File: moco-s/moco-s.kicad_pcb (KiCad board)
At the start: 4 copper layers, 50 x 50 mm, 167 parts, among them J1 Conn_01x07, J2 Conn_01x02, J3 Conn_01x05, J5 Debug, J6 Conn_01x06, J7 Conn_01x03, J8 Conn_02x02_Top_Bottom, J9 Conn_02x02_Top_Bottom, Q1 AO3413, Q2 AO3413, Q3 CSD18540Q5B, Q4 CSD18540Q5B, Q5 CSD18540Q5B, Q6 CSD18540Q5B, Q7 CSD18540Q5B, Q8 CSD18540Q5B, SW1 SW_Push, SW2 SW_Push, U1 AMS1117-3.3, U2 DRV8301, U3 STM32G431CBT6, U4 MCP2515-xST, U5 TJA1051T-3, U6 AS5147, Y1 32.768kHz, Y2 8MHz, Y3 8MHz

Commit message: Update net classes
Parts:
- moved J7 1.50 mm to (147.5, 79.0)
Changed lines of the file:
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@@
   )
   (footprint "moco:AMASS MR30PB-F" (layer "F.Cu")
-    (at 147.5 77.5 -90)
+    (at 147.5 79 -90)
     (property "Note" "J7 connect to motor")
     (property "Sheetfile" "File: motor_driver.kicad_sch")

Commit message: Update layout
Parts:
- removed J6: Conn_01x06, Connector_JST:JST_GH_SM06B-GHS-TB_1x06-1MP_P1.25mm_Horizontal
- removed JP4, JP5, SB15, SB20: SolderJumper_3_Bridged12, Jumper:SolderJumper-3_P1.3mm_Bridged12_RoundedPad1.0x1.5mm_NumberLabels
- removed R19, R20, R21: 3.3k, Resistor_SMD:R_0402_1005Metric
- removed SB14, SB21, SB22: SolderJumper_2_Bridged, Jumper:SolderJumper-2_P1.3mm_Bridged_RoundedPad1.0x1.5mm
- removed TP1, TP2: TestPoint, TestPoint:TestPoint_Pad_D2.0mm
- added R14: 3.3k, Resistor_SMD:R_0402_1005Metric, F.Cu at (95.6, 68.5)
- added R17: 3.3k, Resistor_SMD:R_0402_1005Metric, F.Cu at (91.2, 72.0)
- added R18: 3.3k, Resistor_SMD:R_0402_1005Metric, F.Cu at (94.2, 72.0)
- J3: value Conn_01x05 -> Conn_01x09; footprint Connector_JST:JST_GH_SM05B-GHS-TB_1x05-1MP_P1.25mm_Horizontal -> Connector_JST:JST_GH_SM09B-GHS-TB_1x09-1MP_P1.25mm_Horizontal
- NT2: moved to B.Cu
- SB4: value SolderJumper_3_Bridged12 -> SolderJumper_2_Bridged; footprint Jumper:SolderJumper-3_P1.3mm_Bridged12_RoundedPad1.0x1.5mm_NumberLabels -> Jumper:SolderJumper-2_P1.3mm_Bridged_RoundedPad1.0x1.5mm; moved to F.Cu
- moved SB4 26.6 mm to (92.0, 69.3), turned to 0 degrees
- moved C1 21.1 mm to (160.0, 67.2)
- moved C3 21.1 mm to (160.0, 79.2)
- moved C32 21.1 mm to (160.0, 91.2)
- moved C33 21.1 mm to (160.0, 83.2)
- moved C35 21.1 mm to (160.0, 75.2)
- moved C4 21.1 mm to (160.0, 71.2)
- moved C5 21.1 mm to (160.0, 63.2)
- moved C7 21.1 mm to (160.0, 87.2)
- moved R24 12.2 mm to (142.0, 60.2), turned to 0 degrees
- moved C37 10.5 mm to (125.6, 92.0), turned to 180 degrees
- moved C38 10.4 mm to (125.6, 89.6), turned to 0 degrees
- moved R13 8.73 mm to (121.7, 98.5), turned to 180 degrees
- moved SB7 6.20 mm to (108.8, 94.6)
- moved Y1 6.09 mm to (122.6, 90.8), turned to 90 degrees
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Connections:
- J1 pad 1: Net-(J1-Pad1) -> VCC
- J3 pad 1: Net-(J3-Pad1) -> VCC
- J3 pad 5: GND -> /SPI_CLK
- SB4 pad 1: VCC -> Net-(R14-Pad1)
- SB4 pad 2: Net-(J1-Pad1) -> VCC
- U3 pad 33: /CAN BUS/CNA_RX -> /CAN BUS/~{INT}
- U3 pad 46: /CAN BUS/CNA_TX -> /CAN BUS/SPI_~{CS}
- U4 pad 1: /CAN BUS/MCP_TX -> /CAN BUS/TX
- U4 pad 13: Net-(SB22-Pad1) -> /CAN BUS/~{INT}
- U4 pad 18: Net-(SB21-Pad2) -> /CAN BUS/SPI_~{CS}
- U4 pad 2: /CAN BUS/MCP_RX -> /CAN BUS/RX
- U5 pad 1: /CAN BUS/CAN_TX_TRN -> /CAN BUS/TX
- U5 pad 4: /CAN BUS/CAN_RX_TRN -> /CAN BUS/RX
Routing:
- net GND: track 0.00 -> 79.5 mm, vias 0 -> 35
- net VCC: track 0.00 -> 76.2 mm, vias 0 -> 12
- net /SPI_MOSI: track 0.00 -> 68.5 mm, vias 0 -> 4
- net /ENC_B: track 0.00 -> 59.9 mm, vias 0 -> 2
- net /EN_GATE: track 0.00 -> 58.0 mm, vias 0 -> 3
- net /~{OCTW}: track 0.00 -> 57.3 mm, vias 0 -> 4
- net /ENC_I: track 0.00 -> 55.6 mm, vias 0 -> 2
- net /SPI_CLK: track 0.00 -> 53.8 mm, vias 0 -> 4
- net /ENC_A: track 0.00 -> 51.6 mm, vias 0 -> 2
- net /SPI_MISO: track 0.00 -> 51.1 mm, vias 0 -> 3
- net Vdrive: track 0.00 -> 48.8 mm, vias 0 -> 17
- net /~{FAULT}: track 0.00 -> 47.1 mm, vias 0 -> 3
- net /MCU/TEMP_SENSE: track 0.00 -> 40.7 mm, vias 0 -> 2
- net +5V: track 0.00 -> 39.7 mm, vias 0 -> 2
- net /CAN BUS/SPI_~{CS}: track 0.00 -> 36.5 mm, vias 0 -> 2
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- added copper zone on B.Cu, net /Motor Driver/MOTOR_A
- added copper zone on F.Cu, net /Motor Driver/MOTOR_A
- added copper zone on B.Cu, net /Motor Driver/MOTOR_B
- added copper zone on F.Cu, net /Motor Driver/MOTOR_B
- added copper zone on B.Cu, net /Motor Driver/MOTOR_C
- added copper zone on F.Cu, net /Motor Driver/MOTOR_C
- added copper zone on B.Cu, net /Motor Driver/SL_B
- added copper zone on F.Cu, net /Motor Driver/SL_B
- added copper zone on B.Cu, net /Motor Driver/SL_C
- added copper zone on F.Cu, net /Motor Driver/SL_C
- added copper zone on B.Cu, net GND
- added copper zone on F.Cu, net GND
- added copper zone on In1.Cu, net GND
- added copper zone on B.Cu, net Vdrive
- added copper zone on F.Cu, net Vdrive
- added copper zone on In1.Cu, net Vdrive

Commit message: Comp MoCo-S
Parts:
- removed C37, C38: 12pF, Capacitor_SMD:C_0603_1608Metric
- removed C4: 22uF/50V, Capacitor_SMD:C_1210_3225Metric_Pad1.33x2.70mm_HandSolder
- removed C52: 100nF, Capacitor_SMD:C_0402_1005Metric
- removed C53: 100pF, Capacitor_SMD:C_0402_1005Metric
- removed LD2, LD3, LD4, LD5: LED, LED_SMD:LED_0603_1608Metric
- removed Q1, Q2: AO3413, Package_TO_SOT_SMD:SOT-23
- removed R10, R5: 330R, Resistor_SMD:R_0402_1005Metric
- removed R12, R51: 10k, Resistor_SMD:R_0603_1608Metric
- removed R23: 1k, Resistor_SMD:R_0402_1005Metric
- removed R4, R47, R48, R9: 10k, Resistor_SMD:R_0402_1005Metric
- removed R49: 120R, Resistor_SMD:R_0402_1005Metric
- removed R7: 150R, Resistor_SMD:R_0402_1005Metric
- removed SB1, SB19, SB2, SB3, SB6: SolderJumper_2_Bridged, Jumper:SolderJumper-2_P1.3mm_Bridged_RoundedPad1.0x1.5mm
- removed U5: TJA1051T-3, Package_SO:SOIC-8_3.9x4.9mm_P1.27mm
- removed Y1: 32.768kHz, Crystal:Crystal_SMD_3215-2Pin_3.2x1.5mm
- added R19: 10k, Resistor_SMD:R_0402_1005Metric, F.Cu at (105.9, 95.3)
- added R20: 120R, Resistor_SMD:R_0402_1005Metric, F.Cu at (105.5, 85.2)
- added SB5: SolderJumper_2_Open, Jumper:SolderJumper-2_P1.3mm_Open_TrianglePad1.0x1.5mm, B.Cu at (106.2, 83.5)
- C47, C48: value 12pF -> 100nF
- C50: value 100nF -> 22pF
- C51: value 10uF -> 22pF; footprint Capacitor_Tantalum_SMD:CP_EIA-3216-18_Kemet-A -> Capacitor_SMD:C_0402_1005Metric
- C8: value 10uF -> 4.7uF; footprint Capacitor_Tantalum_SMD:CP_EIA-3216-18_Kemet-A -> Capacitor_SMD:C_0402_1005Metric
- H1, H2: footprint MountingHole:MountingHole_3.2mm_M3_Pad_Via -> MountingHole:MountingHole_2.2mm_M2_Pad_Via
- H3, H4: footprint MountingHole:MountingHole_3.2mm_M3_ISO14580 -> MountingHole:MountingHole_2.2mm_M2_ISO14580
- J1: value Conn_01x07 -> Conn_01x06; footprint Connector_JST:JST_GH_SM07B-GHS-TB_1x07-1MP_P1.25mm_Horizontal -> Connector_JST:JST_GH_SM06B-GHS-TB_1x06-1MP_P1.25mm_Horizontal
- J3, NT2: moved to F.Cu
- J9, SB4: moved to B.Cu
- LD1: value LED -> LED_BAGR; footprint LED_SMD:LED_0603_1608Metric -> moco:RGB LED 1.6x1.6mm
- R1: value 1k -> 560R
- R2: value 1k -> 330R
- R3: value 150R -> 330R
- U1: value AMS1117-3.3 -> XC6220B331MR; footprint Package_TO_SOT_SMD:SOT-223-3_TabPin2 -> Package_TO_SOT_SMD:SOT-23-5
- U4: value MCP2515-xST -> MCP25625; footprint Package_SO:TSSOP-20_4.4x6.5mm_P0.65mm -> Package_DFN_QFN:QFN-28-1EP_6x6mm_P0.65mm_EP4.25x4.25mm
- Y3: value 8MHz -> 16MHz; footprint Crystal:Crystal_SMD_Qantek_QC5CB-2Pin_5x3.2mm -> Crystal:Crystal_SMD_3225-4Pin_3.2x2.5mm
- moved R2 45.5 mm to (109.0, 98.2), turned to 0 degrees
- moved R3 40.7 mm to (109.0, 99.2), turned to 0 degrees
- moved R11 36.7 mm to (107.7, 63.1), turned to 180 degrees
- moved R6 35.0 mm to (107.7, 64.4), turned to 180 degrees
- moved C5 34.7 mm to (133.4, 85.6)
- moved C33 32.3 mm to (134.2, 63.8)
- moved SB7 30.9 mm to (109.5, 63.8), turned to 180 degrees
- moved C1 30.3 mm to (132.2, 79.3)
- moved C3 28.0 mm to (132.2, 75.9)
- moved C35 27.0 mm to (134.2, 67.2)
- moved C7 25.2 mm to (134.9, 89.9), turned to -90 degrees
- moved J1 23.4 mm to (103.2, 63.1)
- moved C32 21.8 mm to (138.2, 89.9), turned to -90 degrees
- moved R17 20.0 mm to (107.7, 60.6), turned to 180 degrees
- moved SB4 19.5 mm to (109.5, 60.6)
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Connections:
- net /GPIO_PB13 renamed /SPI_DRIVER_~{CS}
- net /GPIO_PB14 renamed /SPI_SENSOR_~{CS}
- C47 pad 1: GND -> VCC
- C47 pad 2: Net-(C47-Pad2) -> GND
- C48 pad 1: Net-(C48-Pad1) -> VCC
- C49 pad 1: VCC -> +5V
- C50 pad 1: VCC -> Net-(C50-Pad1)
- C51 pad 1: +5V -> GND
- C51 pad 2: GND -> Net-(C51-Pad2)
- J1 pad 4: /GPIO_PB0 -> /GPIO_PB2
- J1 pad 5: /GPIO_PB1 -> /GPIO_PB11
- J1 pad 6: /GPIO_PB2 -> GND
- J5 pad 3: GND -> /SWDIO
- J5 pad 4: /SWDIO -> GND
- LD1 pad 1: GND -> Net-(LD1-Pad1)
- LD1 pad 2: Net-(LD1-Pad2) -> +5V
- R1 pad 1: Net-(R1-Pad1) -> Net-(LD1-Pad4)
- R1 pad 2: Net-(LD1-Pad2) -> /USER_LED_1
- R2 pad 1: Net-(R2-Pad1) -> Net-(LD1-Pad3)
- R2 pad 2: Net-(LD2-Pad2) -> GND
- R3 pad 1: Net-(Q1-Pad1) -> Net-(LD1-Pad1)
- R3 pad 2: /~{OCTW} -> /USER_LED_2
- R31 pad 1: /~{OCTW} -> /Motor Driver/~{OCTW}
- U1 pad 1: GND -> +5V
- U1 pad 2: VCC -> GND
- U2 pad 5: /~{OCTW} -> /Motor Driver/~{OCTW}
- U3 pad 16: /GPIO_PB0 -> /USER_LED_1
- U3 pad 17: /GPIO_PB1 -> /USER_LED_2
- U3 pad 25: /~{OCTW} -> /GPIO_PB11
- U3 pad 3: Net-(C37-Pad2) -> unconnected-(U3-Pad3)
- U3 pad 4: Net-(C38-Pad1) -> unconnected-(U3-Pad4)
- U3 pad 46: /CAN BUS/SPI_~{CS} -> /SPI_CAN_~{CS}
- U4 pad 1: /CAN BUS/TX -> VCC
- U4 pad 15: unconnected-(U4-Pad15) -> /SPI_MOSI
- U4 pad 16: /SPI_MOSI -> /SPI_MISO
- U4 pad 17: /SPI_MISO -> /SPI_CAN_~{CS}
- U4 pad 18: /CAN BUS/SPI_~{CS} -> Net-(R19-Pad2)
- U4 pad 19: Net-(R47-Pad2) -> VCC
- U4 pad 2: /CAN BUS/RX -> unconnected-(U4-Pad2)
- U4 pad 20: VCC -> Net-(U4-Pad20)
- U4 pad 3: unconnected-(U4-Pad3) -> /CAN BUS/CAN_L
- U4 pad 4: unconnected-(U4-Pad4) -> /CAN BUS/CAN_H
- U4 pad 5: unconnected-(U4-Pad5) -> GND
- U4 pad 8: Net-(C47-Pad2) -> Net-(C50-Pad1)
- U4 pad 9: Net-(C48-Pad1) -> Net-(C51-Pad2)
- Y3 pad 1: Net-(C47-Pad2) -> Net-(C51-Pad2)
- Y3 pad 2: Net-(C48-Pad1) -> GND
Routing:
- net VCC: track 76.2 -> 261.9 mm, vias 12 -> 18
- net +5V: track 39.7 -> 110.7 mm, vias 2 -> 4
- net /~{OCTW}: track 57.3 -> 0.00 mm, vias 4 -> 0
- net /I2C_SDA: track 2.13 -> 50.9 mm, vias 0 -> 4
- net /GPIO_PB11: track 0.00 -> 43.0 mm, vias 0 -> 2
- net /I2C_SCL: track 1.92 -> 42.3 mm, vias 0 -> 3
- net /GPIO_PB2: track 7.61 -> 46.8 mm, vias 1 -> 2
- net /CAN BUS/SPI_~{CS}: track 36.5 -> 0.00 mm, vias 2 -> 0
- net /OnBoard_ENC_A: track 0.00 -> 32.3 mm, vias 0 -> 3
- net /SPI_CLK: track 53.8 -> 86.0 mm, vias 4 -> 5
- net /OnBoard_ENC_B: track 0.00 -> 31.6 mm, vias 0 -> 3
- net /SPI_MISO: track 51.1 -> 81.1 mm, vias 3 -> 5
- net /ENC_B: track 59.9 -> 32.0 mm
- net GND: track 79.5 -> 107.1 mm, vias 35 -> 107
- net /CAN BUS/CAN_L: track 21.0 -> 47.9 mm
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- removed copper zone on B.Cu, net /Motor Driver/SL_B
- removed copper zone on B.Cu, net /Motor Driver/SL_C
- removed copper zone on In1.Cu, net Vdrive

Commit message: Update ref
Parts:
- renumbered C2 to C1, C15 to C10, C16 to C11, C17 to C12, C18 to C13, C19 to C14, C20 to C15, C21 to C16, C22 to C17, C23 to C18, C24 to C19, C6 to C2, C25 to C20, C26 to C21, C27 to C22, C28 to C23, C29 to C24, C30 to C25, C36 to C26, C31 to C27, C5 to C28, C7 to C29, C8 to C3, C32 to C30, C33 to C31, C35 to C32, C34 to C33, C1 to C34, C3 to C35, C39 to C36, C40 to C37, C41 to C38, C42 to C39, C9 to C4, C43 to C40, C44 to C41, C45 to C42, C46 to C43, C47 to C44, C48 to C45, C49 to C46, C50 to C47, C51 to C48, C54 to C49, C10 to C5, C55 to C50, C11 to C6, C12 to C7, C13 to C8, C14 to C9, H3 to H1, H1 to H2, H4 to H3, H2 to H4, J5 to J2, J2 to J3, J3 to J4, J7 to J5, J8 to J6, J9 to J7, Q3 to Q1, Q4 to Q2, Q5 to Q3, Q6 to Q4, Q7 to Q5, Q8 to Q6, R6 to R1, R14 to R10, R17 to R11, R18 to R12, R24 to R13, R25 to R14, R26 to R15, R27 to R16, R28 to R17, R29 to R18, R30 to R19, R8 to R2, R31 to R20, R32 to R21, R33 to R22, R34 to R23, R35 to R24, R36 to R25, R37 to R26, R38 to R27, R39 to R28, R40 to R29, R11 to R3, R41 to R30, R42 to R31, R43 to R32, R44 to R33, R45 to R34, R46 to R35, R19 to R36, R20 to R37, R52 to R38, R15 to R4, R16 to R5, R13 to R6, R1 to R7, R2 to R8, R3 to R9, SB7 to SB1, JP1 to SB2, JP2 to SB3, JP3 to SB4, SB4 to SB5, SB5 to SB6, TP3 to TP1, TP5 to TP2, TP4 to TP3, U6 to U5, Y2 to Y1, Y3 to Y2

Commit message: Update layout
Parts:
- added kibuzzard-638C8B7C: G***, kibuzzard-638C8B7C, B.Cu at (139.7, 59.2)
- added kibuzzard-638C8BCF: G***, kibuzzard-638C8BCF, B.Cu at (132.6, 58.7)
- added kibuzzard-638C8E29: G***, kibuzzard-638C8E29, B.Cu at (109.9, 72.4)
- added kibuzzard-638C8E4D: G***, kibuzzard-638C8E4D, B.Cu at (111.5, 75.2)
- moved C2 0.25 mm to (117.9, 52.4)
- moved C3 0.25 mm to (117.9, 54.6)
- moved U1 0.25 mm to (115.6, 53.5)
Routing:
- net VCC: track 261.9 -> 259.0 mm
- net GND: track 107.1 -> 104.5 mm, vias 107 -> 118
- net Net-(C19-Pad2): track 22.7 -> 21.6 mm
- net Vdrive: track 48.7 -> 49.2 mm, vias 122 -> 133
- net /Motor Driver/MOTOR_B: track 25.1 -> 24.8 mm, vias 43 -> 49
- net /Motor Driver/MOTOR_C: vias 43 -> 50
- net /Motor Driver/MOTOR_A: vias 43 -> 50
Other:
- outline, holes or cut-outs redrawn

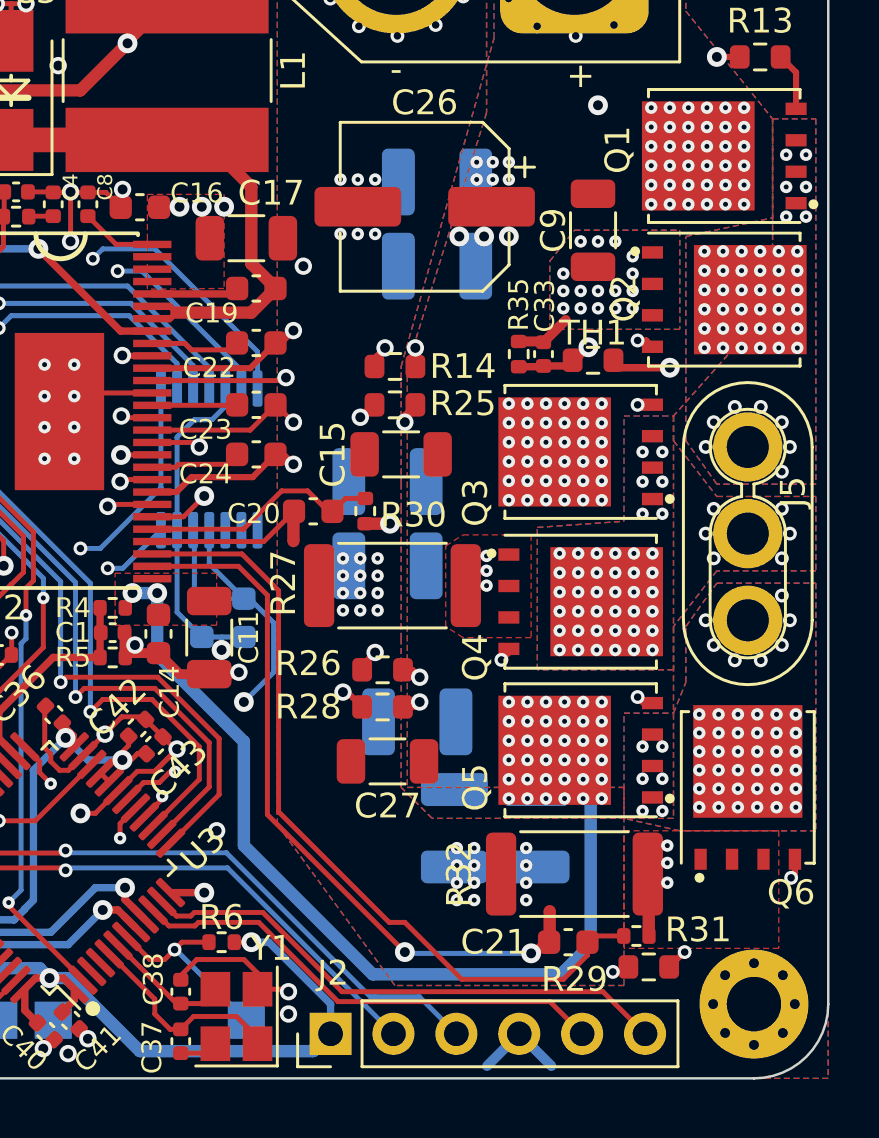
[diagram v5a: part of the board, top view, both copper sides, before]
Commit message: Use kelvin connection for shunt resistance
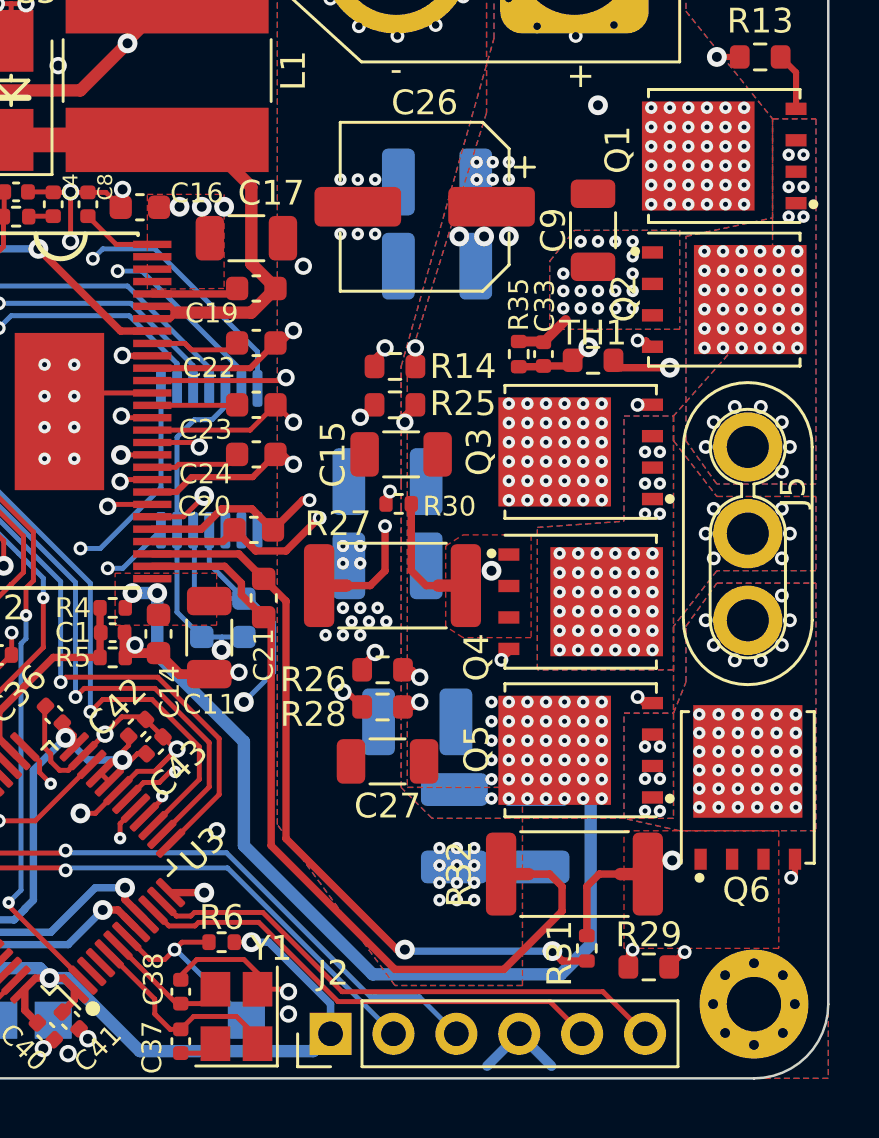
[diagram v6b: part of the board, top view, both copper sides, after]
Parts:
- C43: value 1uF/25V -> 1uF
- moved C21 18.6 mm to (127.2, 80.6), turned to -90 degrees
- moved NT1 3.87 mm to (134.8, 80.1)
- moved NT2 2.83 mm to (130.1, 80.1), turned to 180 degrees
- moved C20 2.51 mm to (126.8, 77.8)
- moved NT4 2.41 mm to (137.4, 91.8), turned to 180 degrees
- moved R31 2.06 mm to (140.2, 94.8), turned to 90 degrees
- moved NT3 1.87 mm to (142.1, 91.8), turned to 0 degrees
- moved R30 1.38 mm to (132.7, 76.8), turned to 0 degrees
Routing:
- net /Motor Driver/SP1: track 6.44 -> 14.2 mm, vias 0 -> 2
- net /Motor Driver/SP2: track 27.9 -> 32.3 mm, vias 2 -> 0
- net /Motor Driver/SN1: track 0.00 -> 4.04 mm
- net /Motor Driver/SN2: track 0.00 -> 3.55 mm
- net Net-(C21-Pad1): track 32.4 -> 30.0 mm, vias 0 -> 2
- net /Motor Driver/GL_C: track 37.5 -> 35.5 mm
- net Net-(C20-Pad1): track 9.80 -> 11.5 mm, vias 0 -> 2
- net /Motor Driver/SL_C: track 31.3 -> 29.7 mm, vias 4 -> 2
- net /GPIO_PB2: track 46.7 -> 47.5 mm
- net /Motor Driver/SL_B: track 19.9 -> 20.1 mm, vias 5 -> 2
- net Vdrive: vias 133 -> 139
- net GND: vias 118 -> 120
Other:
- board text added: "${TITLE} v${REVISION}"

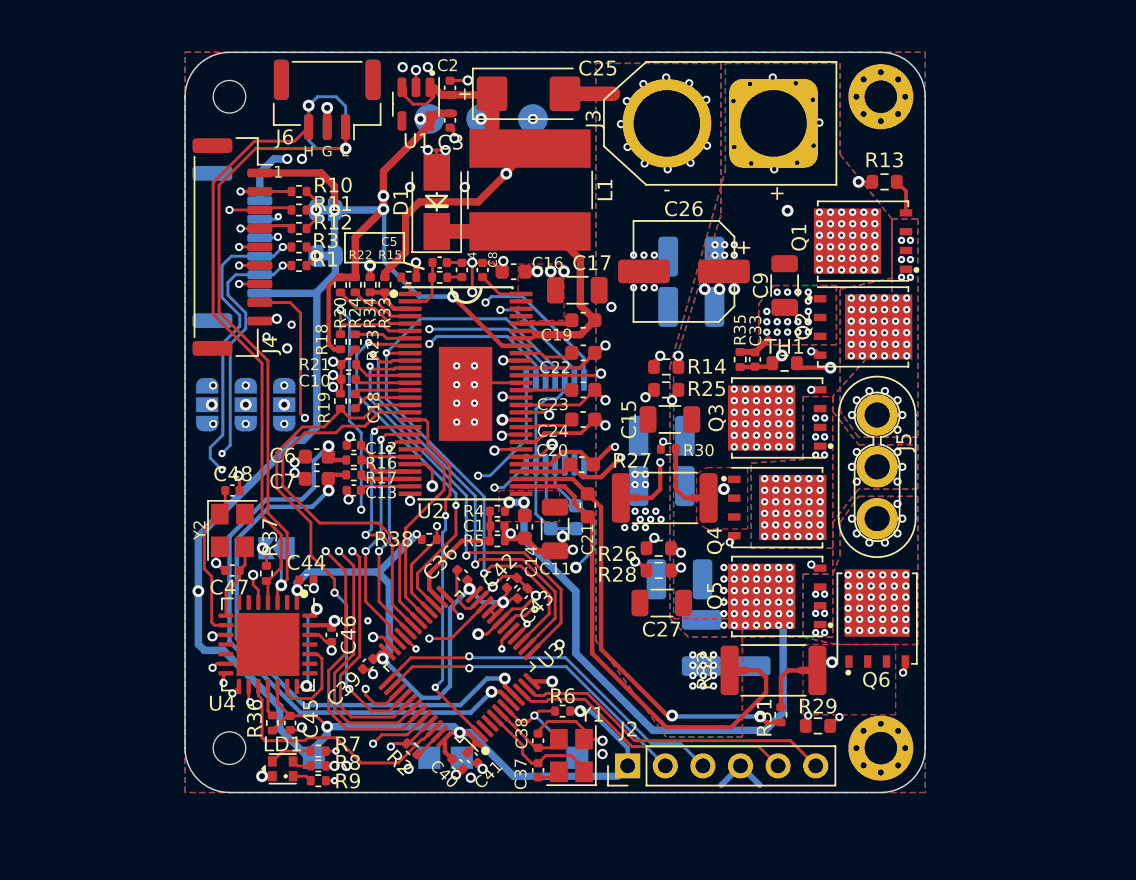
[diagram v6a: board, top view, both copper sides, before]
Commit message: Replace some extended parts to basic parts
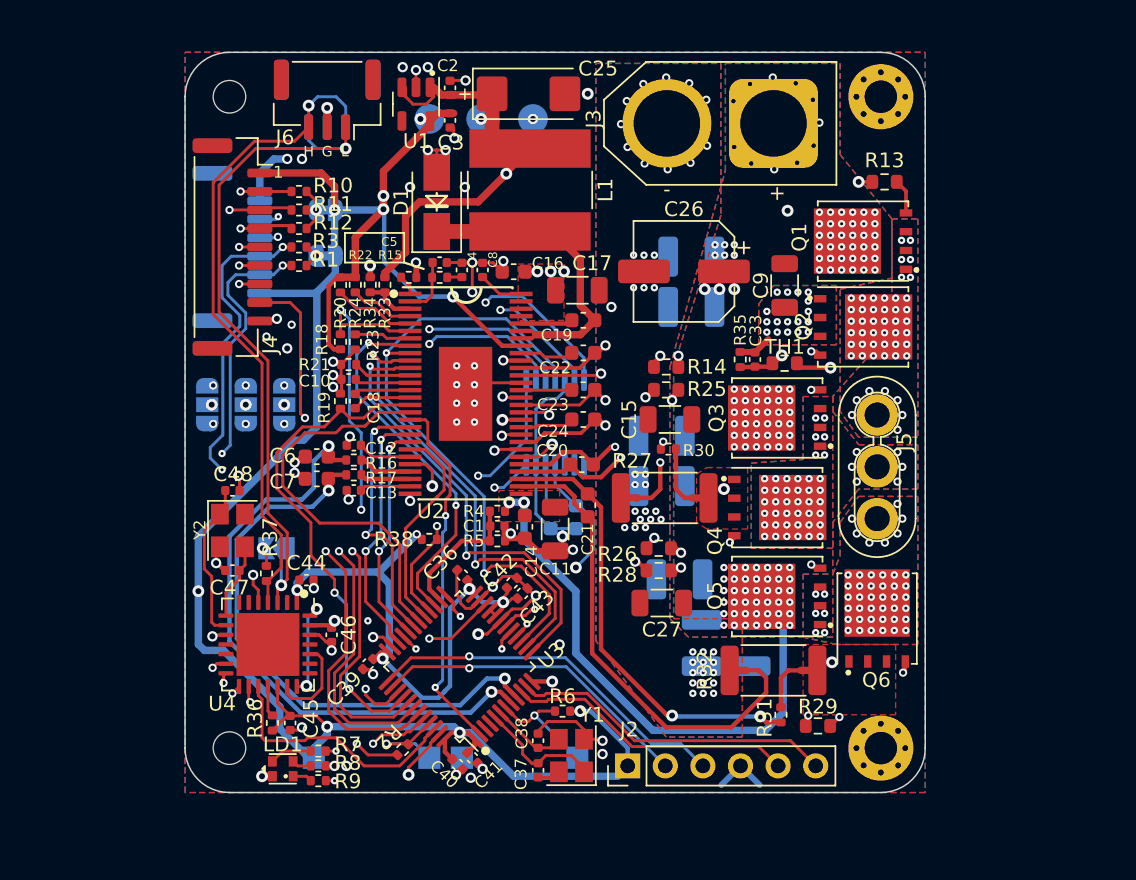
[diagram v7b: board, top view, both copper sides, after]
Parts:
- C10, C33: value 2.2uF -> 2.2uF/16V
- C15, C27, C9: value 2.2uF/100V -> 2.2uF/50V
- R7: value 560R -> 680R
- moved R2 0.63 mm to (114.7, 97.1), turned to -135 degrees
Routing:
- net GND: track 104.5 -> 105.7 mm, vias 120 -> 125
- net /MCU_BOOT0: track 6.32 -> 6.92 mm
